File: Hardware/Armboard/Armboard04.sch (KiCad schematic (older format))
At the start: 0 parts

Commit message: Added, Solenoid actuation, laser control, and encoders
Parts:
- added Conn? (x6): Molex_SL_03, symbol MRDT_Connectors:Molex_SL_03
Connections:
- new net +3V3: Conn?.1, Conn?.1, Conn?.1, Conn?.1, Conn?.1, Conn?.1
- new net GND: Conn?.2, Conn?.2, Conn?.2, Conn?.2, Conn?.2, Conn?.2
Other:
- note added: "Enc_1"
- note added: "Enc_2"
- note added: "Enc_3"
- note added: "Enc_4"
- note added: "Enc_5"
- note added: "Enc_6"

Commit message: H-Bridge completed
Completed the H-Bridge Hierarchal Sheet
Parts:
- Conn? (x6): symbol MRDT_Connectors:Molex_SL_03 -> Armboard-rescue:Molex_SL_03-MRDT_Connectors
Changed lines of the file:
@@
 $EndDescr
 $Comp
-L MRDT_Connectors:Molex_SL_03 Conn?
+L Armboard-rescue:Molex_SL_03-MRDT_Connectors Conn?
 U 1 1 5F78DE1F
 P 3750 3090
@@
 Enc_1
 $Comp
-L MRDT_Connectors:Molex_SL_03 Conn?
+L Armboard-rescue:Molex_SL_03-MRDT_Connectors Conn?
 U 1 1 5F78F4A7
 P 3790 4120
@@
 Enc_2
 $Comp
-L MRDT_Connectors:Molex_SL_03 Conn?
+L Armboard-rescue:Molex_SL_03-MRDT_Connectors Conn?
 U 1 1 5F78F9EB
 P 3800 5180
@@
 Enc_3
 $Comp
-L MRDT_Connectors:Molex_SL_03 Conn?
+L Armboard-rescue:Molex_SL_03-MRDT_Connectors Conn?
 U 1 1 5F793695
 P 6700 3080
@@
 Enc_4
 $Comp
-L MRDT_Connectors:Molex_SL_03 Conn?
+L Armboard-rescue:Molex_SL_03-MRDT_Connectors Conn?
 U 1 1 5F7936AB
 P 6740 4110
@@
 Enc_5
 $Comp
-L MRDT_Connectors:Molex_SL_03 Conn?
+L Armboard-rescue:Molex_SL_03-MRDT_Connectors Conn?
 U 1 1 5F7936C1
 P 6750 5170

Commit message: Added serial pins, limit switches, titles, and indicators
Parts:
- removed Conn?: Molex_SL_03, symbol Armboard-rescue:Molex_SL_03-MRDT_Connectors
- added Conn?: Molex_SL_03, symbol Armboard-rescue:Molex_SL_03-MRDT_Connectors-Armboard-rescue
- added D? (x6): LED, symbol Device:LED
- added R? (x6): 330, symbol Device:R
- Conn? (x5): symbol Armboard-rescue:Molex_SL_03-MRDT_Connectors -> Armboard-rescue:Molex_SL_03-MRDT_Connectors-Armboard-rescue
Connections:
- net labels added: Enc_1_PWM, Enc_2_PWM, Enc_3_PWM, Enc_4_PWM, Enc_5_PWM, Enc_6_PWM
- wire segments 18 -> 48
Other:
- note added: "Encoders"
- note added: "Yellow"

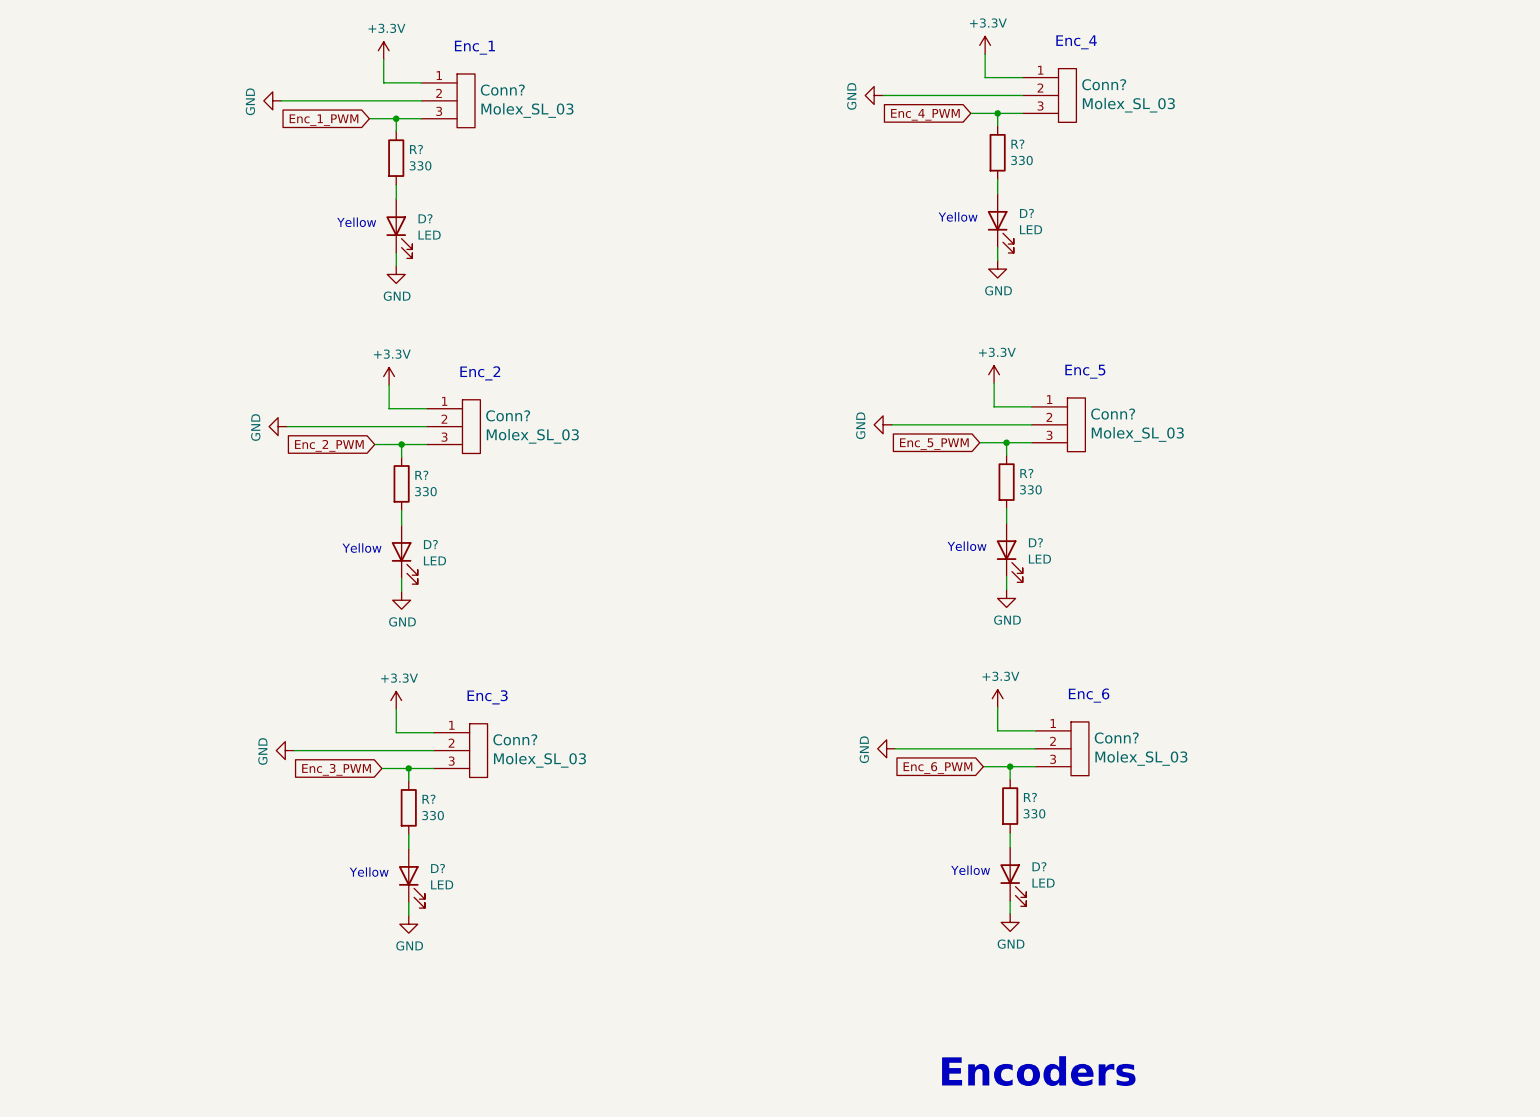
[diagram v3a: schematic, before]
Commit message: Formatted GNDs and added motor toggle buttons
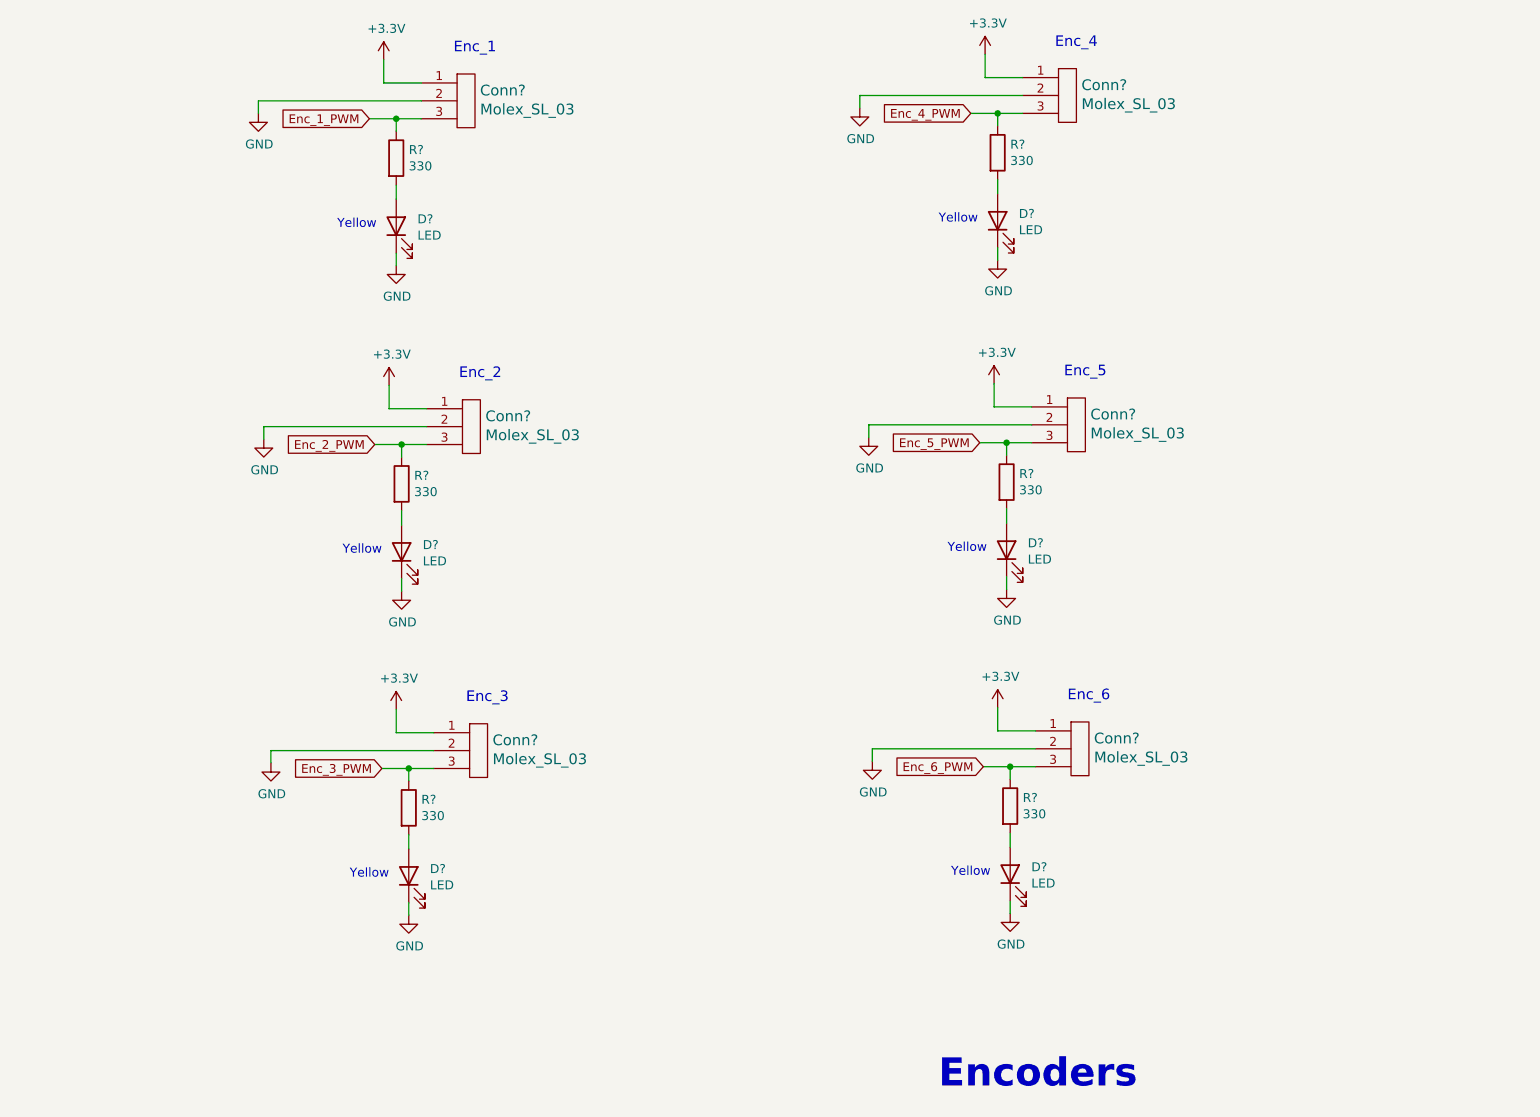
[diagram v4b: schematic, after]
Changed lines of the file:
@@
 L power:GND #PWR?
 U 1 1 5F845545
-P 2830 1620
-F 0 "#PWR?" H 2830 1370 50  0001 C CNN
-F 1 "GND" H 2835 1447 50  0000 C CNN
-F 2 "" H 2830 1620 50  0001 C CNN
-F 3 "" H 2830 1620 50  0001 C CNN
-	1    2830 1620
-	0    1    1    0
+P 2700 1690
+F 0 "#PWR?" H 2700 1440 50  0001 C CNN
+F 1 "GND" H 2705 1517 50  0000 C CNN
+F 2 "" H 2700 1690 50  0001 C CNN
+F 3 "" H 2700 1690 50  0001 C CNN
+	1    2700 1690
+	1    0    0    -1
 $EndComp
 Text Notes 3790 1360 0    59   ~ 0
@@
 Text GLabel 3320 1720 0    49   Input ~ 0
 Enc_1_PWM
-Wire Wire Line
-	2830 1620 3610 1620
 $Comp
 L Device:R R?
@@
 Yellow
 $Comp
-L power:GND #PWR?
-U 1 1 5F84C9DB
-P 2860 3440
-F 0 "#PWR?" H 2860 3190 50  0001 C CNN
-F 1 "GND" H 2865 3267 50  0000 C CNN
-F 2 "" H 2860 3440 50  0001 C CNN
-F 3 "" H 2860 3440 50  0001 C CNN
-	1    2860 3440
-	0    1    1    0
-$EndComp
-Text GLabel 3350 3540 0    49   Input ~ 0
-Enc_2_PWM
-Wire Wire Line
-	2860 3440 3640 3440
-$Comp
 L Device:R R?
 U 1 1 5F84C9E3
@@
 Text Notes 3170 4160 0    50   ~ 0
 Yellow
-$Comp
-L power:GND #PWR?
-U 1 1 5F8509BE
-P 2900 5250
-F 0 "#PWR?" H 2900 5000 50  0001 C CNN
-F 1 "GND" H 2905 5077 50  0000 C CNN
-F 2 "" H 2900 5250 50  0001 C CNN
-F 3 "" H 2900 5250 50  0001 C CNN
-	1    2900 5250
-	0    1    1    0
-$EndComp
 Text GLabel 3390 5350 0    49   Input ~ 0
 Enc_3_PWM
-Wire Wire Line
-	2900 5250 3680 5250
 $Comp
 L Device:R R?
@@
 Text Notes 3210 5970 0    50   ~ 0
 Yellow
-$Comp
-L power:GND #PWR?
-U 1 1 5F855852
-P 6190 1590
-F 0 "#PWR?" H 6190 1340 50  0001 C CNN
-F 1 "GND" H 6195 1417 50  0000 C CNN
-F 2 "" H 6190 1590 50  0001 C CNN
-F 3 "" H 6190 1590 50  0001 C CNN
-	1    6190 1590
-	0    1    1    0
-$EndComp
 Text GLabel 6680 1690 0    49   Input ~ 0
 Enc_4_PWM
-Wire Wire Line
-	6190 1590 6970 1590
 $Comp
 L Device:R R?
@@
 Text Notes 6500 2310 0    50   ~ 0
 Yellow
-$Comp
-L power:GND #PWR?
-U 1 1 5F8564D4
-P 6240 3430
-F 0 "#PWR?" H 6240 3180 50  0001 C CNN
-F 1 "GND" H 6245 3257 50  0000 C CNN
-F 2 "" H 6240 3430 50  0001 C CNN
-F 3 "" H 6240 3430 50  0001 C CNN
-	1    6240 3430
-	0    1    1    0
-$EndComp
 Text GLabel 6730 3530 0    49   Input ~ 0
 Enc_5_PWM
-Wire Wire Line
-	6240 3430 7020 3430
 $Comp
 L Device:R R?
@@
 Text Notes 6550 4150 0    50   ~ 0
 Yellow
-$Comp
-L power:GND #PWR?
-U 1 1 5F857291
-P 6260 5240
-F 0 "#PWR?" H 6260 4990 50  0001 C CNN
-F 1 "GND" H 6265 5067 50  0000 C CNN
-F 2 "" H 6260 5240 50  0001 C CNN
-F 3 "" H 6260 5240 50  0001 C CNN
-	1    6260 5240
-	0    1    1    0
-$EndComp
 Text GLabel 6750 5340 0    49   Input ~ 0
 Enc_6_PWM
-Wire Wire Line
-	6260 5240 7040 5240
 $Comp
 L Device:R R?
@@
 Text Notes 6570 5960 0    50   ~ 0
 Yellow
+Wire Wire Line
+	2700 1620 2700 1690
+Wire Wire Line
+	2700 1620 3610 1620
+Text GLabel 3350 3540 0    49   Input ~ 0
+Enc_2_PWM
+$Comp
+L power:GND #PWR?
+U 1 1 5F84A43A
+P 2730 3510
+F 0 "#PWR?" H 2730 3260 50  0001 C CNN
+F 1 "GND" H 2735 3337 50  0000 C CNN
+F 2 "" H 2730 3510 50  0001 C CNN
+F 3 "" H 2730 3510 50  0001 C CNN
+	1    2730 3510
+	1    0    0    -1
+$EndComp
+Wire Wire Line
+	2730 3440 2730 3510
+Wire Wire Line
+	2730 3440 3640 3440
+$Comp
+L power:GND #PWR?
+U 1 1 5F84B8CF
+P 2770 5320
+F 0 "#PWR?" H 2770 5070 50  0001 C CNN
+F 1 "GND" H 2775 5147 50  0000 C CNN
+F 2 "" H 2770 5320 50  0001 C CNN
+F 3 "" H 2770 5320 50  0001 C CNN
+	1    2770 5320
+	1    0    0    -1
+$EndComp
+Wire Wire Line
+	2770 5250 2770 5320
+Wire Wire Line
+	2770 5250 3680 5250
+$Comp
+L power:GND #PWR?
+U 1 1 5F84CEAD
+P 6060 1660
+F 0 "#PWR?" H 6060 1410 50  0001 C CNN
+F 1 "GND" H 6065 1487 50  0000 C CNN
+F 2 "" H 6060 1660 50  0001 C CNN
+F 3 "" H 6060 1660 50  0001 C CNN
+	1    6060 1660
+	1    0    0    -1
+$EndComp
+Wire Wire Line
+	6060 1590 6060 1660
+Wire Wire Line
+	6060 1590 6970 1590
+$Comp
+L power:GND #PWR?
+U 1 1 5F84E5D5
+P 6110 3500
+F 0 "#PWR?" H 6110 3250 50  0001 C CNN
+F 1 "GND" H 6115 3327 50  0000 C CNN
+F 2 "" H 6110 3500 50  0001 C CNN
+F 3 "" H 6110 3500 50  0001 C CNN
+	1    6110 3500
+	1    0    0    -1
+$EndComp
+Wire Wire Line
+	6110 3430 6110 3500
+Wire Wire Line
+	6110 3430 7020 3430
+$Comp
+L power:GND #PWR?
+U 1 1 5F84FDBC
+P 6130 5310
+F 0 "#PWR?" H 6130 5060 50  0001 C CNN
+F 1 "GND" H 6135 5137 50  0000 C CNN
+F 2 "" H 6130 5310 50  0001 C CNN
+F 3 "" H 6130 5310 50  0001 C CNN
+	1    6130 5310
+	1    0    0    -1
+$EndComp
+Wire Wire Line
+	6130 5240 6130 5310
+Wire Wire Line
+	6130 5240 7040 5240
 $EndSCHEMATC

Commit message: Fixed buttons/switches page, changed resistor values, fixed some tiva connections
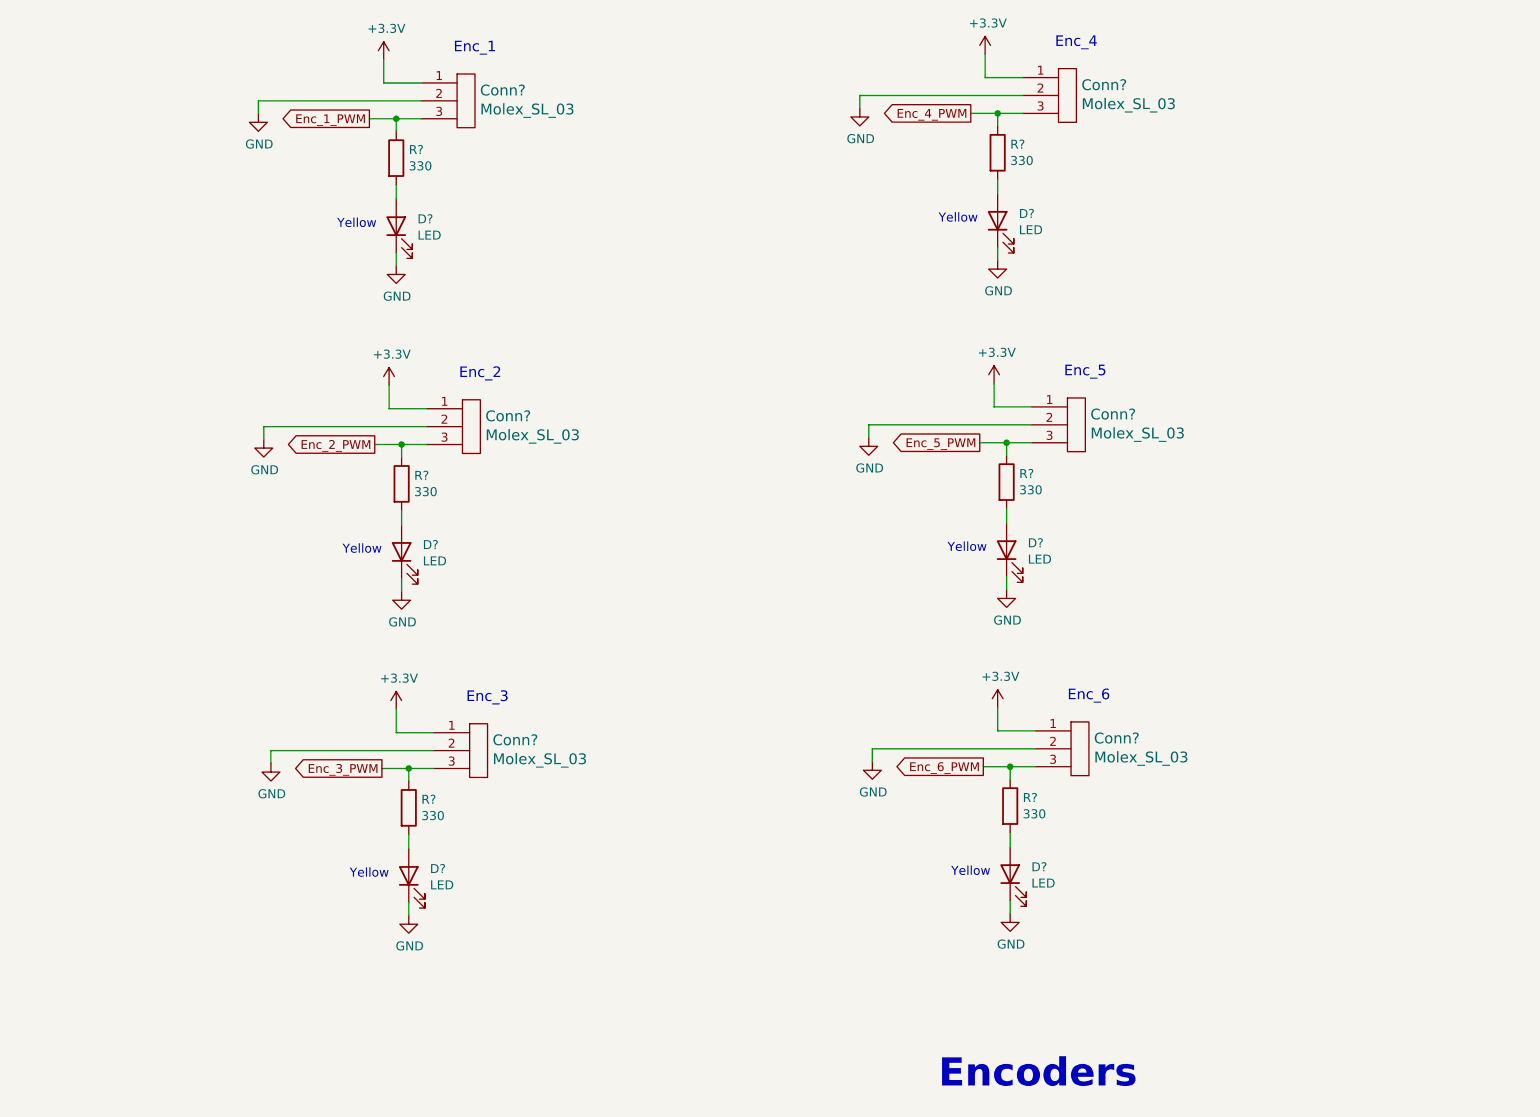
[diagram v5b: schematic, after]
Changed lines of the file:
@@
 Text Notes 3790 1360 0    59   ~ 0
 Enc_1
-Text GLabel 3320 1720 0    49   Input ~ 0
+Text GLabel 3320 1720 0    49   Output ~ 0
 Enc_1_PWM
 $Comp
@@
 Text Notes 3170 4160 0    50   ~ 0
 Yellow
-Text GLabel 3390 5350 0    49   Input ~ 0
+Text GLabel 3390 5350 0    49   Output ~ 0
 Enc_3_PWM
 $Comp
@@
 Text Notes 3210 5970 0    50   ~ 0
 Yellow
-Text GLabel 6680 1690 0    49   Input ~ 0
+Text GLabel 6680 1690 0    49   Output ~ 0
 Enc_4_PWM
 $Comp
@@
 Text Notes 6500 2310 0    50   ~ 0
 Yellow
-Text GLabel 6730 3530 0    49   Input ~ 0
+Text GLabel 6730 3530 0    49   Output ~ 0
 Enc_5_PWM
 $Comp
@@
 Text Notes 6550 4150 0    50   ~ 0
 Yellow
-Text GLabel 6750 5340 0    49   Input ~ 0
+Text GLabel 6750 5340 0    49   Output ~ 0
 Enc_6_PWM
 $Comp
@@
 Wire Wire Line
 	2700 1620 3610 1620
-Text GLabel 3350 3540 0    49   Input ~ 0
+Text GLabel 3350 3540 0    49   Output ~ 0
 Enc_2_PWM
 $Comp
